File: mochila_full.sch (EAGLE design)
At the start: 13 parts, among them IC1 AD620R

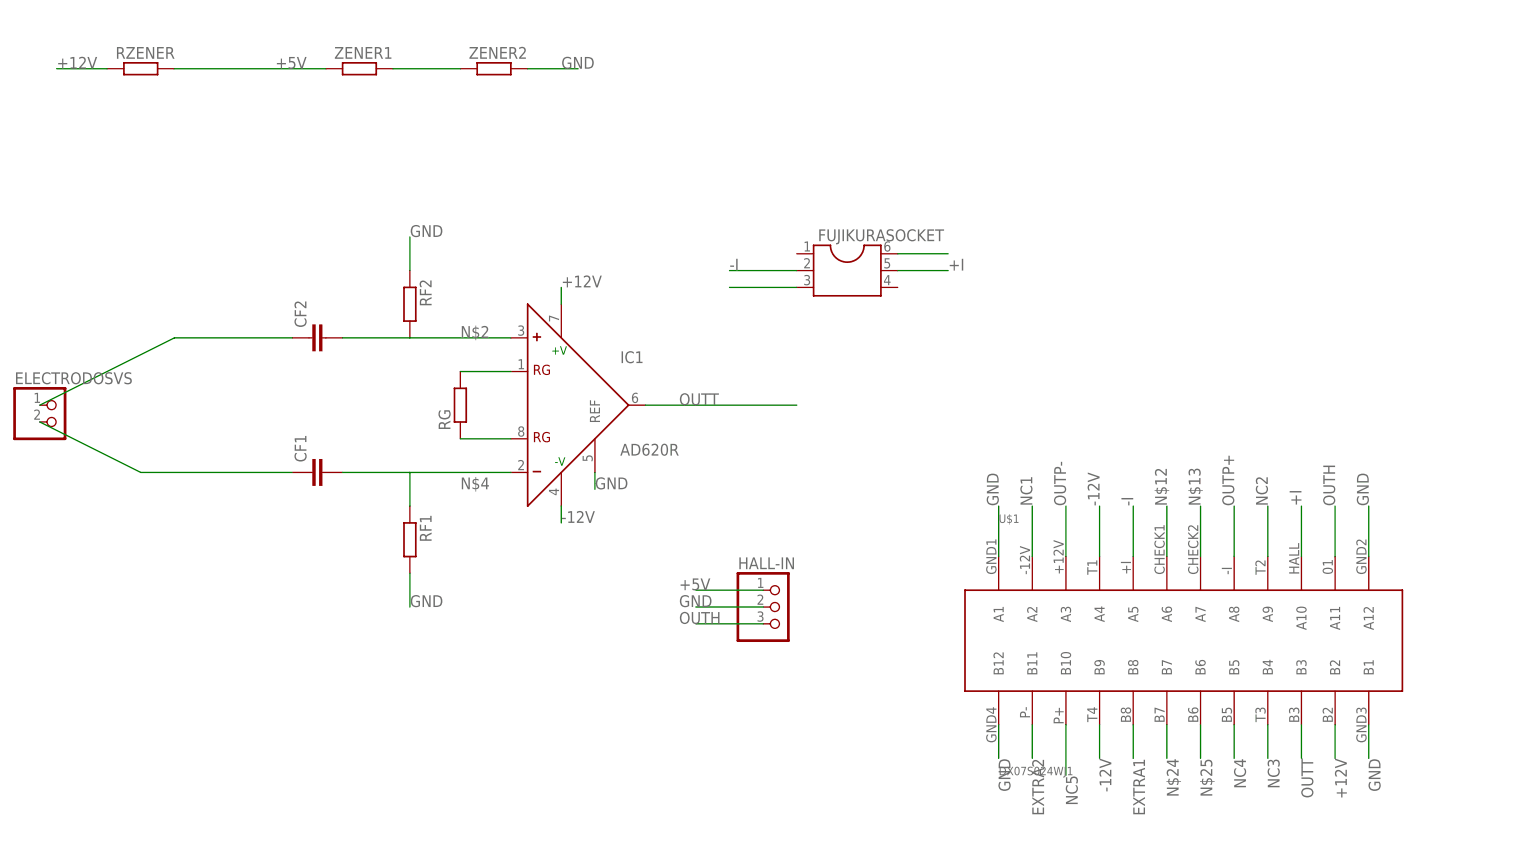
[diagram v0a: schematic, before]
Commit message: Corregimos placa de conexion universal y mochila
Esta version se envia a imprimir
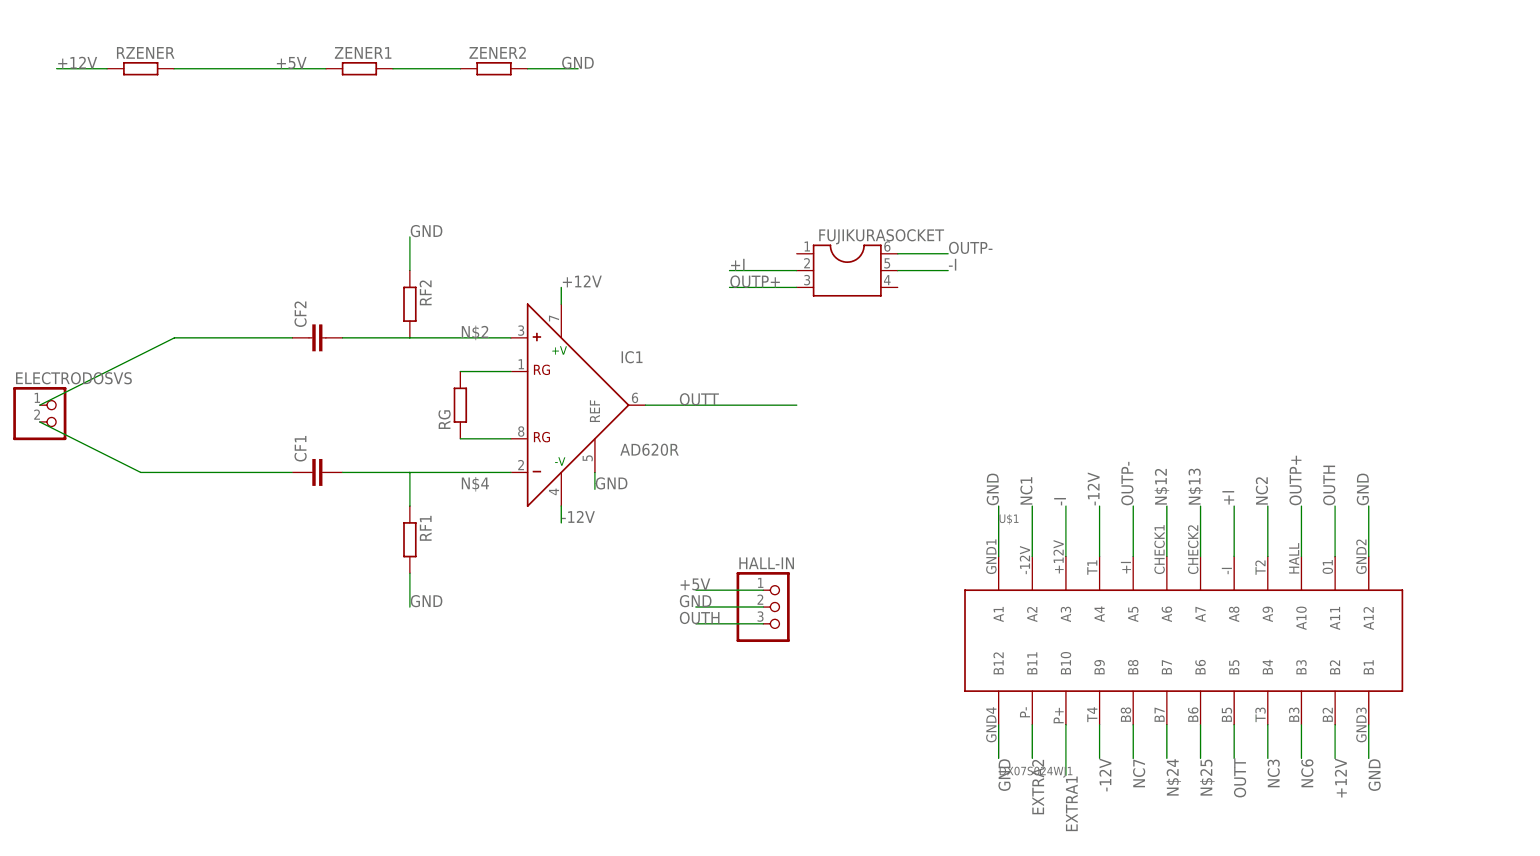
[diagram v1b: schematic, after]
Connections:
- removed net NC4: U$1.B5
- removed net NC5: U$1.B10
- new net NC6: U$1.B3
- new net NC7: U$1.B8
- net +I: now also FUJIKURASOCKET.2, U$1.A8; no longer FUJIKURASOCKET.5, U$1.A10
- net -I: now also FUJIKURASOCKET.5, U$1.A3; no longer FUJIKURASOCKET.2, U$1.A5
- net EXTRA1: now also U$1.B10; no longer U$1.B8
- net OUTP+: now also FUJIKURASOCKET.3, U$1.A10; no longer FUJIKURASOCKET.6, U$1.A8
- net OUTP-: now also FUJIKURASOCKET.6, U$1.A5; no longer FUJIKURASOCKET.3, U$1.A3
- net OUTT: now also U$1.B5; no longer U$1.B3
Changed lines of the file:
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@@
 </segment>
 <segment>
-<pinref part="U$1" gate="G$1" pin="B3"/>
-<wire x1="172.72" y1="10.16" x2="172.72" y2="5.08" width="0.1524" layer="91"/>
-<label x="172.72" y="5.08" size="1.778" layer="95" rot="R270"/>
+<pinref part="U$1" gate="G$1" pin="B5"/>
+<wire x1="162.56" y1="10.16" x2="162.56" y2="5.08" width="0.1524" layer="91"/>
+<label x="162.56" y="5.08" size="1.778" layer="95" rot="R270"/>
 </segment>
 </net>
 <net name="+I" class="0">
 <segment>
-<pinref part="FUJIKURASOCKET" gate="G$1" pin="5"/>
-<wire x1="111.76" y1="78.74" x2="119.38" y2="78.74" width="0.1524" layer="91"/>
-<label x="119.38" y="78.74" size="1.778" layer="95"/>
+<pinref part="FUJIKURASOCKET" gate="G$1" pin="2"/>
+<wire x1="96.52" y1="78.74" x2="86.36" y2="78.74" width="0.1524" layer="91"/>
+<label x="86.36" y="78.74" size="1.778" layer="95"/>
 </segment>
 <segment>
-<pinref part="U$1" gate="G$1" pin="A10"/>
-<wire x1="172.72" y1="35.56" x2="172.72" y2="43.18" width="0.1524" layer="91"/>
-<label x="172.72" y="43.18" size="1.778" layer="95" rot="R90"/>
+<pinref part="U$1" gate="G$1" pin="A8"/>
+<wire x1="162.56" y1="35.56" x2="162.56" y2="43.18" width="0.1524" layer="91"/>
+<label x="162.56" y="43.18" size="1.778" layer="95" rot="R90"/>
 </segment>
 </net>
@@
 <net name="-I" class="0">
 <segment>
-<pinref part="FUJIKURASOCKET" gate="G$1" pin="2"/>
-<wire x1="96.52" y1="78.74" x2="86.36" y2="78.74" width="0.1524" layer="91"/>
-<label x="86.36" y="78.74" size="1.778" layer="95"/>
+<pinref part="FUJIKURASOCKET" gate="G$1" pin="5"/>
+<wire x1="111.76" y1="78.74" x2="119.38" y2="78.74" width="0.1524" layer="91"/>
+<label x="119.38" y="78.74" size="1.778" layer="95"/>
 </segment>
 <segment>
-<pinref part="U$1" gate="G$1" pin="A5"/>
-<wire x1="147.32" y1="35.56" x2="147.32" y2="43.18" width="0.1524" layer="91"/>
-<label x="147.32" y="43.18" size="1.778" layer="95" rot="R90"/>
+<pinref part="U$1" gate="G$1" pin="A3"/>
+<wire x1="137.16" y1="35.56" x2="137.16" y2="43.18" width="0.1524" layer="91"/>
+<label x="137.16" y="43.18" size="1.778" layer="95" rot="R90"/>
 </segment>
 </net>
@@
 <net name="OUTP-" class="0">
 <segment>
-<pinref part="U$1" gate="G$1" pin="A3"/>
-<wire x1="137.16" y1="35.56" x2="137.16" y2="43.18" width="0.1524" layer="91"/>
-<label x="137.16" y="43.18" size="1.778" layer="95" rot="R90"/>
+<pinref part="FUJIKURASOCKET" gate="G$1" pin="6"/>
+<wire x1="111.76" y1="81.28" x2="119.38" y2="81.28" width="0.1524" layer="91"/>
+<label x="119.38" y="81.28" size="1.778" layer="95"/>
 </segment>
 <segment>
-<pinref part="FUJIKURASOCKET" gate="G$1" pin="3"/>
-<wire x1="96.52" y1="76.2" x2="86.36" y2="76.2" width="0.1524" layer="91"/>
+<pinref part="U$1" gate="G$1" pin="A5"/>
+<wire x1="147.32" y1="35.56" x2="147.32" y2="43.18" width="0.1524" layer="91"/>
+<label x="147.32" y="43.18" size="1.778" layer="95" rot="R90"/>
 </segment>
 </net>
 <net name="OUTP+" class="0">
 <segment>
-<pinref part="U$1" gate="G$1" pin="A8"/>
-<wire x1="162.56" y1="35.56" x2="162.56" y2="43.18" width="0.1524" layer="91"/>
-<label x="162.56" y="43.18" size="1.778" layer="95" rot="R90"/>
+<pinref part="FUJIKURASOCKET" gate="G$1" pin="3"/>
+<wire x1="96.52" y1="76.2" x2="86.36" y2="76.2" width="0.1524" layer="91"/>
+<label x="86.36" y="76.2" size="1.778" layer="95"/>
 </segment>
 <segment>
-<pinref part="FUJIKURASOCKET" gate="G$1" pin="6"/>
-<wire x1="111.76" y1="81.28" x2="119.38" y2="81.28" width="0.1524" layer="91"/>
+<pinref part="U$1" gate="G$1" pin="A10"/>
+<wire x1="172.72" y1="35.56" x2="172.72" y2="43.18" width="0.1524" layer="91"/>
+<label x="172.72" y="43.18" size="1.778" layer="95" rot="R90"/>
 </segment>
 </net>
-<net name="EXTRA1" class="0">
+<net name="NC7" class="0">
 <segment>
 <pinref part="U$1" gate="G$1" pin="B8"/>
@@
 </segment>
 </net>
-<net name="NC5" class="0">
-<segment>
-<pinref part="U$1" gate="G$1" pin="B10"/>
-<wire x1="137.16" y1="10.16" x2="137.16" y2="2.54" width="0.1524" layer="91"/>
-<label x="137.16" y="2.54" size="1.778" layer="95" rot="R270"/>
-</segment>
-</net>
 <net name="NC1" class="0">
 <segment>
@@
 <wire x1="132.08" y1="35.56" x2="132.08" y2="43.18" width="0.1524" layer="91"/>
 <label x="132.08" y="43.18" size="1.778" layer="95" rot="R90"/>
-</segment>
-</net>
-<net name="NC4" class="0">
-<segment>
-<pinref part="U$1" gate="G$1" pin="B5"/>
-<wire x1="162.56" y1="10.16" x2="162.56" y2="5.08" width="0.1524" layer="91"/>
-<label x="162.56" y="5.08" size="1.778" layer="95" rot="R270"/>
 </segment>
 </net>
@@
 </segment>
 </net>
+<net name="NC6" class="0">
+<segment>
+<pinref part="U$1" gate="G$1" pin="B3"/>
+<wire x1="172.72" y1="10.16" x2="172.72" y2="5.08" width="0.1524" layer="91"/>
+<label x="172.72" y="5.08" size="1.778" layer="95" rot="R270"/>
+</segment>
+</net>
+<net name="EXTRA1" class="0">
+<segment>
+<pinref part="U$1" gate="G$1" pin="B10"/>
+<wire x1="137.16" y1="10.16" x2="137.16" y2="2.54" width="0.1524" layer="91"/>
+<label x="137.16" y="2.54" size="1.778" layer="95" rot="R270"/>
+</segment>
+</net>

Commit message: Con nueva version de la libreria
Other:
- moved on the sheet: U$1

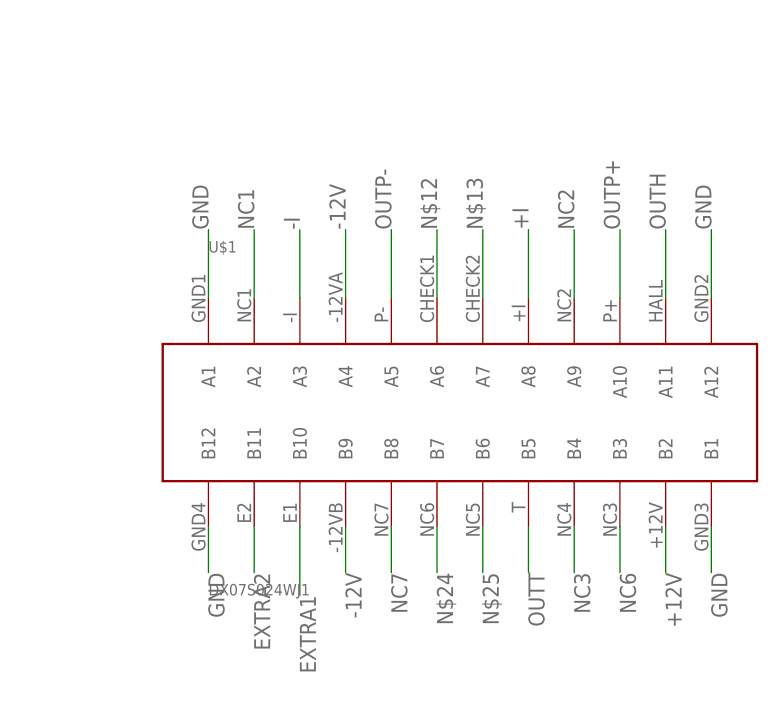
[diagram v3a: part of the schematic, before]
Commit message: Usamos nueva libreria USBC
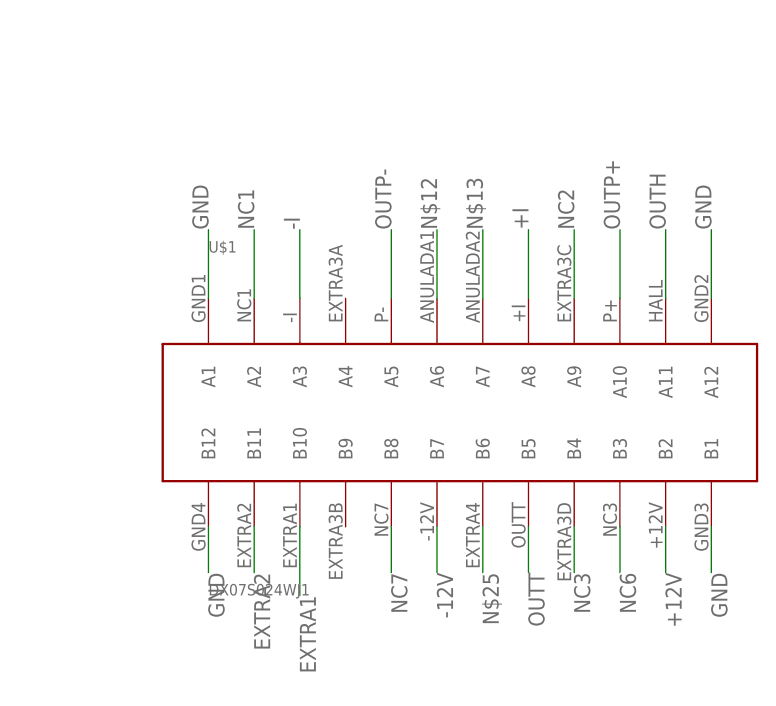
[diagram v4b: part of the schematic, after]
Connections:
- removed net N$24: U$1.B7
- net -12V: now also U$1.B7; no longer U$1.A4, U$1.B9
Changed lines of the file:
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@@
 </segment>
 <segment>
-<pinref part="U$1" gate="G$1" pin="A4"/>
-<wire x1="142.24" y1="35.56" x2="142.24" y2="43.18" width="0.1524" layer="91"/>
-<label x="142.24" y="43.18" size="1.778" layer="95" rot="R90"/>
-</segment>
-<segment>
-<pinref part="U$1" gate="G$1" pin="B9"/>
-<wire x1="142.24" y1="10.16" x2="142.24" y2="5.08" width="0.1524" layer="91"/>
-<label x="142.24" y="5.08" size="1.778" layer="95" rot="R270"/>
+<pinref part="U$1" gate="G$1" pin="B7"/>
+<wire x1="152.4" y1="10.16" x2="152.4" y2="5.08" width="0.1524" layer="91"/>
+<label x="152.4" y="5.08" size="1.778" layer="95" rot="R270"/>
 </segment>
 </net>
@@
 </segment>
 </net>
-<net name="N$24" class="0">
-<segment>
-<pinref part="U$1" gate="G$1" pin="B7"/>
-<wire x1="152.4" y1="10.16" x2="152.4" y2="5.08" width="0.1524" layer="91"/>
-<label x="152.4" y="5.08" size="1.778" layer="95" rot="R270"/>
-</segment>
-</net>

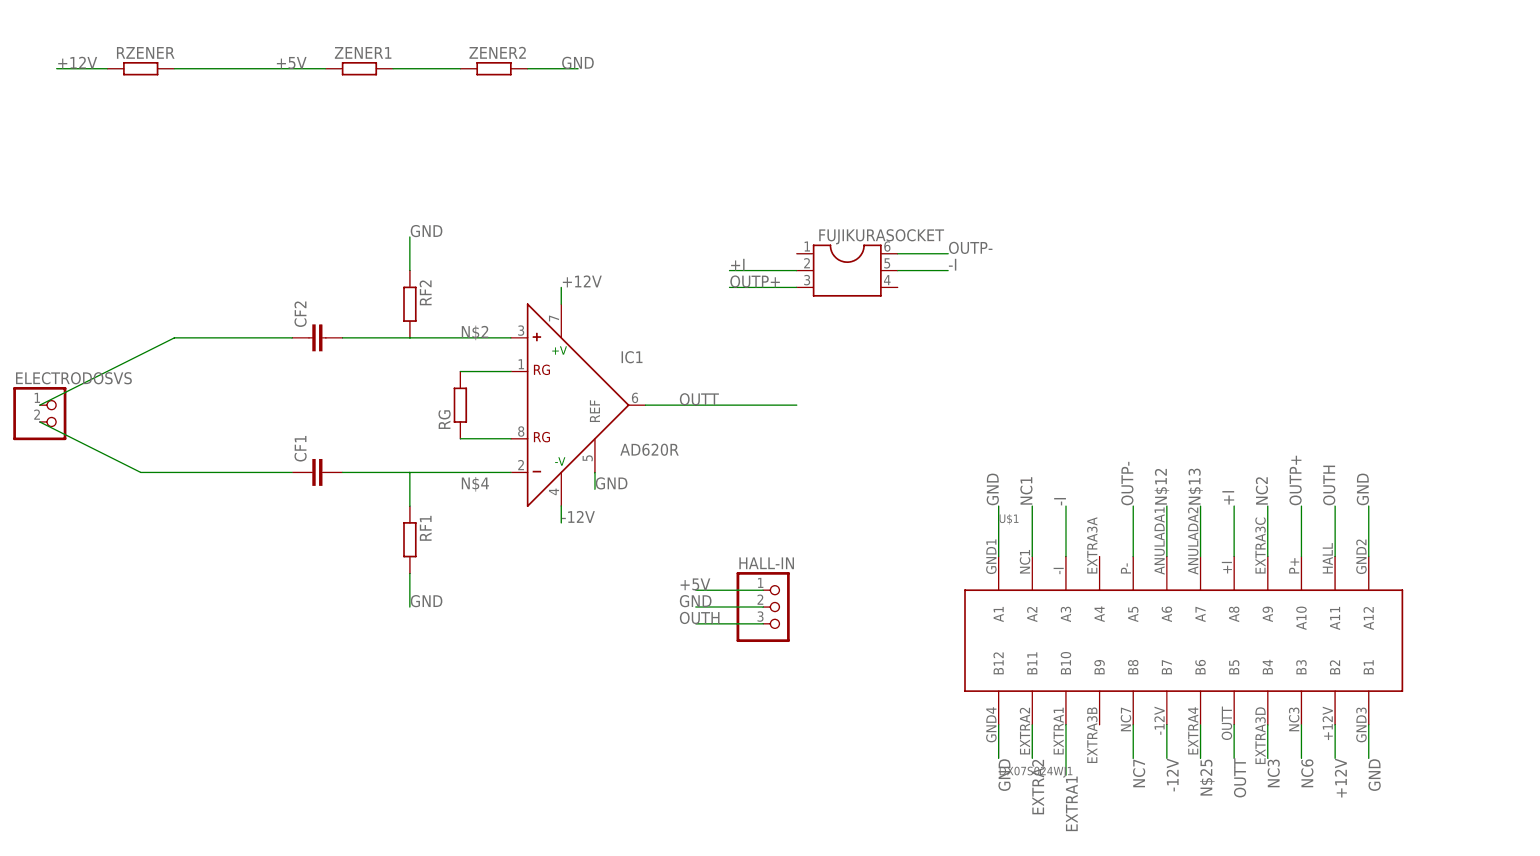
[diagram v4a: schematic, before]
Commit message: Version p/imprimir en masa
Reemplazo los zener por regulador 78L05

Agrego nombres y valores al layout
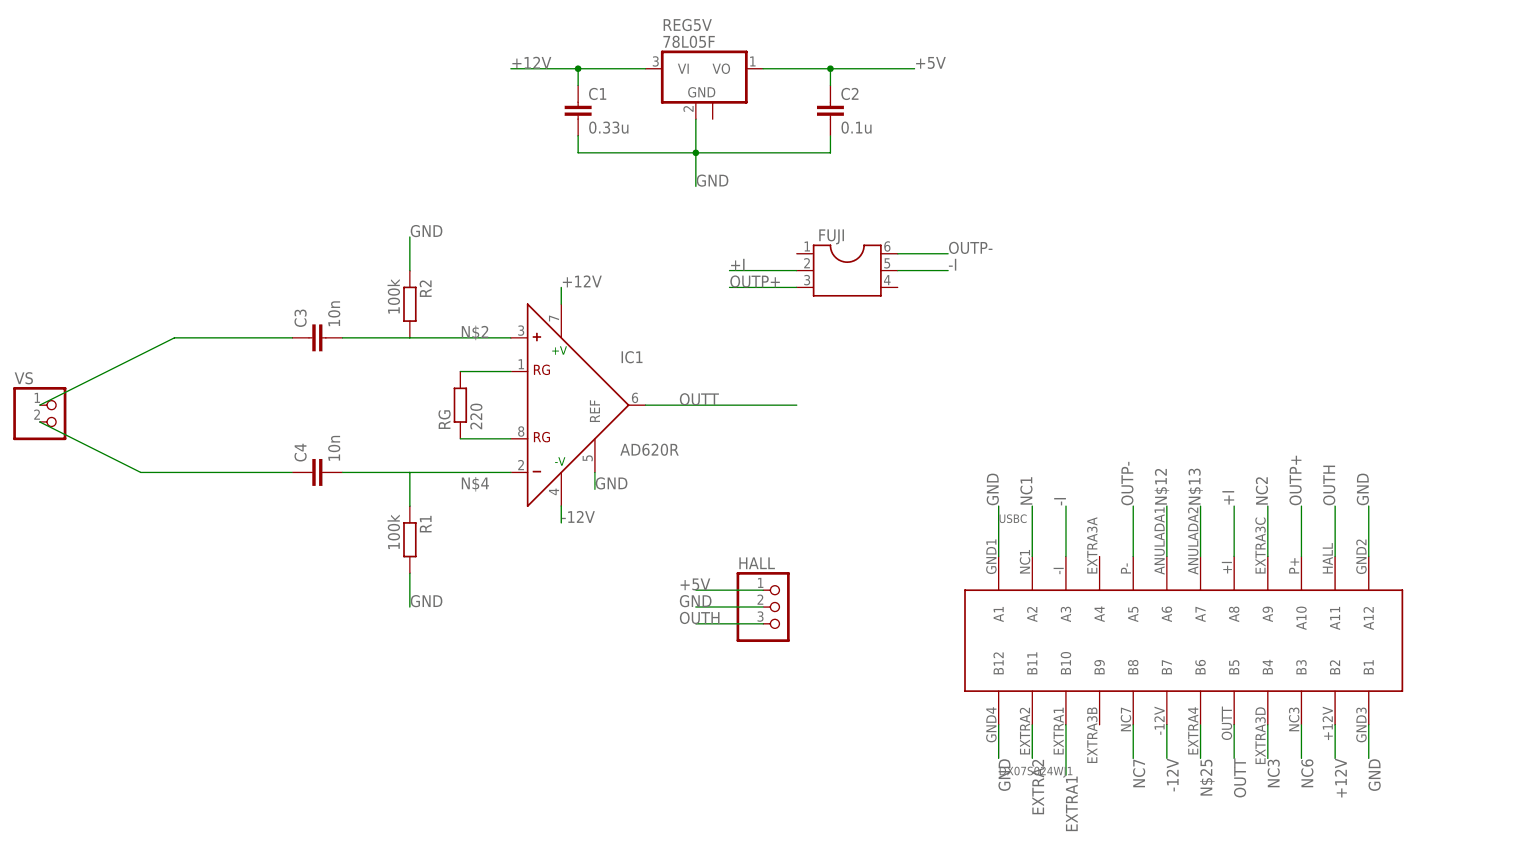
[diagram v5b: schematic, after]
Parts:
- removed RZENER: (no value), eagle-ltspice:R
- removed ZENER1, ZENER2: (no value), eagle-ltspice:RR1206
- added C1: 0.33u, rcl:C-EUC0805
- added C2: 0.1u, rcl:C-EUC0805
- added REG5V: 78L05F, linear:78L05F
- C3, C4: value (none) -> 10n
- R1, R2: value (none) -> 100k
- RG: value (none) -> 220
- renumbered CF1 to C4, CF2 to C3, ELECTRODOSVS to VS, FUJIKURASOCKET to FUJI, HALL-IN to HALL, RF1 to R1, RF2 to R2, U$1 to USBC
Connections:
- removed net N$8: ZENER1.2, ZENER2.1
- net +12V: now also C1.1, REG5V.VI; no longer RZENER.1
- net +5V: now also C2.1, REG5V.VO; no longer RZENER.2, ZENER1.1
- net GND: now also C1.2, C2.2, REG5V.GND; no longer ZENER2.2

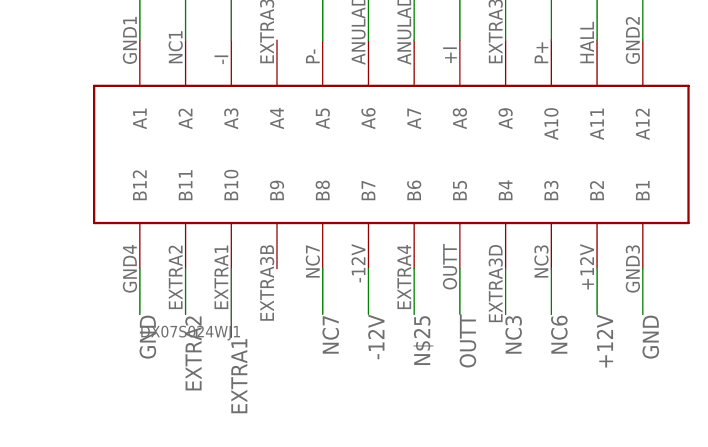
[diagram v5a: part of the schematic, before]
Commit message: Version para imprimir de la mochila, con gerbers generados en .zip
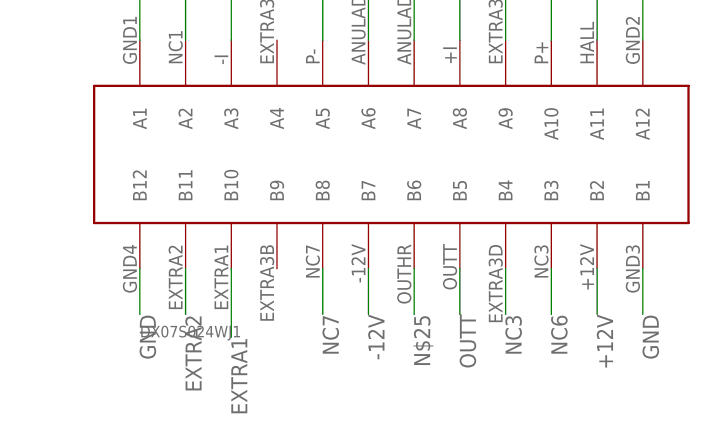
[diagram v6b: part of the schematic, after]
